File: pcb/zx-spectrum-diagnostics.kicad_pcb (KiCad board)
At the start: 2 copper layers, 13 parts, among them J101 Conn_01x04, U101 Pico, U102 Pico

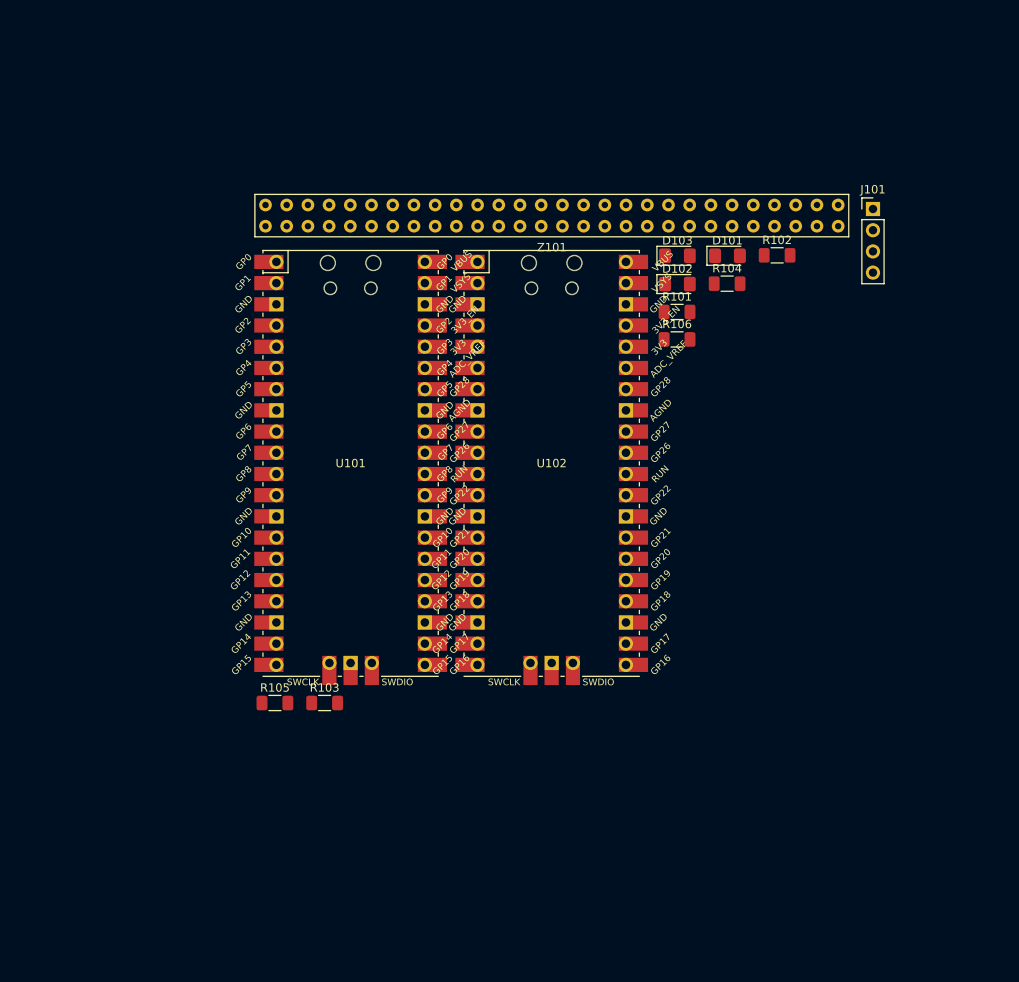
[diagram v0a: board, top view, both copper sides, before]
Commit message: back out previous layout, rearrange connections to match edge connector
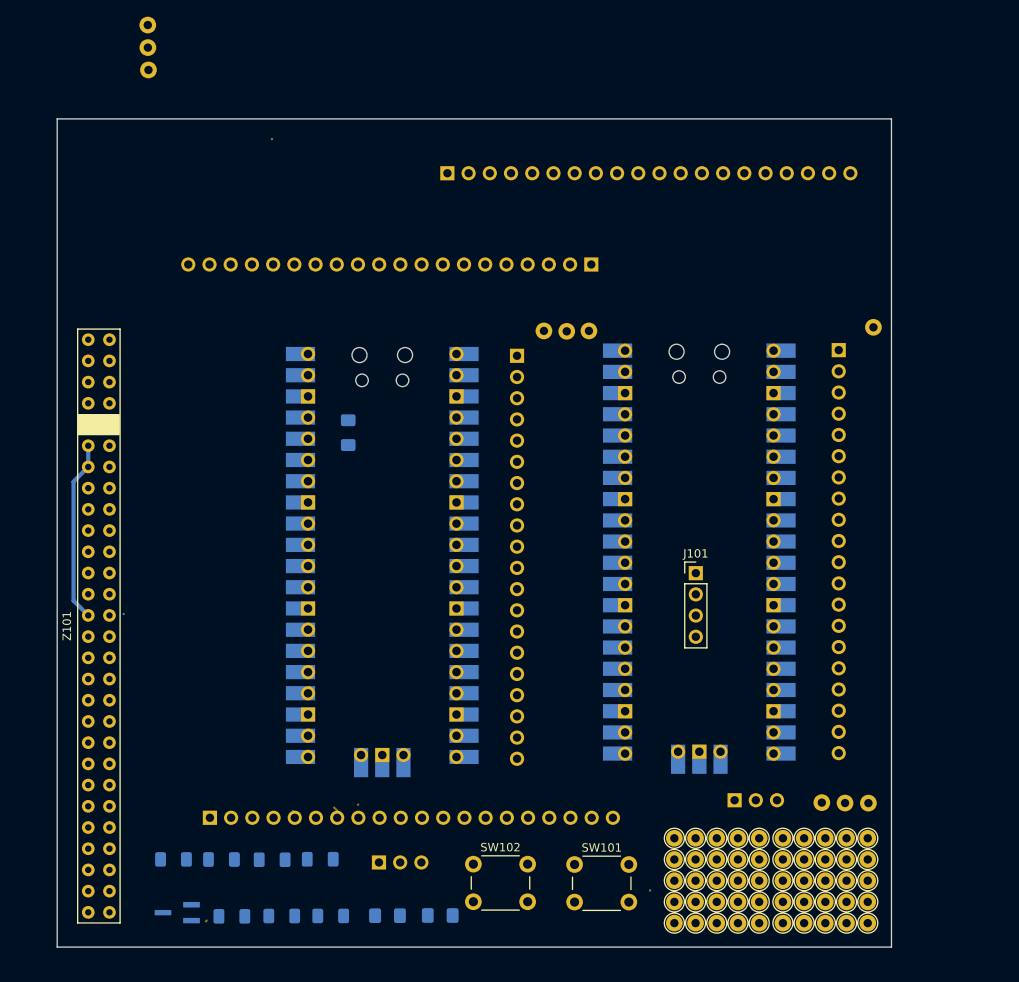
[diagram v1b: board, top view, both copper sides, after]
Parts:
- added ?: , , F.Cu at (133.0, 80.3)
- added ?: , , F.Cu at (172.4, 79.8)
- added ?: , , F.Cu at (85.6, 49.0)
- added ?: , , F.Cu at (166.3, 136.8)
- added ?: , , F.Cu at (85.5, 43.6)
- added ?: , , F.Cu at (171.8, 136.8)
- added ?: , , F.Cu at (138.4, 80.3)
- added ?: , , F.Cu at (135.7, 80.3)
- added ?: , , F.Cu at (169.1, 136.8)
- added ?: , , F.Cu at (85.6, 46.3)
- added J102: Conn_01x03_Male, Connector_PinSocket_2.54mm:PinSocket_1x03_P2.54mm_Vertical, B.Cu at (155.8, 136.5)
- added J103: Conn_01x03_Male, Connector_PinSocket_2.54mm:PinSocket_1x03_P2.54mm_Vertical, B.Cu at (113.2, 143.9)
- added J201: Conn_01x20_Female, Connector_PinSocket_2.54mm:PinSocket_1x20_P2.54mm_Vertical, B.Cu at (138.7, 72.3)
- added J202: Conn_01x20_Female, Connector_PinSocket_2.54mm:PinSocket_1x20_P2.54mm_Vertical, B.Cu at (93.0, 138.6)
- added J203: Conn_01x20_Female, Connector_PinSocket_2.54mm:PinSocket_1x20_P2.54mm_Vertical, B.Cu at (121.4, 61.4)
- added J204: Conn_01x20_Female, Connector_PinSocket_2.54mm:PinSocket_1x20_P2.54mm_Vertical, B.Cu at (168.3, 82.6)
- added J205: Conn_01x20_Female, Connector_PinSocket_2.54mm:PinSocket_1x20_P2.54mm_Vertical, B.Cu at (129.8, 83.2)
- added Q101: PMBT2222A, Package_TO_SOT_SMD:TSOT-23_HandSoldering, B.Cu at (89.1, 149.9)
- added R107: 1K, Resistor_SMD:R_1206_3216Metric_Pad1.30x1.75mm_HandSolder, B.Cu at (95.6, 150.4)
- added REF**: TestPoint_THTPad_D2.0mm_Drill1.0mm, TestPoint:TestPoint_THTPad_D2.0mm_Drill1.0mm, F.Cu at (148.6, 141.0)
- added REF**: TestPoint_THTPad_D2.0mm_Drill1.0mm, TestPoint:TestPoint_THTPad_D2.0mm_Drill1.0mm, F.Cu at (161.6, 141.0)
- added REF**1: TestPoint_THTPad_D2.0mm_Drill1.0mm, TestPoint:TestPoint_THTPad_D2.0mm_Drill1.0mm, F.Cu at (151.2, 141.0)
- added REF**1: TestPoint_THTPad_D2.0mm_Drill1.0mm, TestPoint:TestPoint_THTPad_D2.0mm_Drill1.0mm, F.Cu at (164.2, 141.0)
- added REF**10: TestPoint_THTPad_D2.0mm_Drill1.0mm, TestPoint:TestPoint_THTPad_D2.0mm_Drill1.0mm, F.Cu at (148.6, 146.1)
- added REF**10: TestPoint_THTPad_D2.0mm_Drill1.0mm, TestPoint:TestPoint_THTPad_D2.0mm_Drill1.0mm, F.Cu at (161.6, 146.1)
- added REF**11: TestPoint_THTPad_D2.0mm_Drill1.0mm, TestPoint:TestPoint_THTPad_D2.0mm_Drill1.0mm, F.Cu at (164.2, 146.1)
- added REF**11: TestPoint_THTPad_D2.0mm_Drill1.0mm, TestPoint:TestPoint_THTPad_D2.0mm_Drill1.0mm, F.Cu at (151.2, 146.1)
- added REF**12: TestPoint_THTPad_D2.0mm_Drill1.0mm, TestPoint:TestPoint_THTPad_D2.0mm_Drill1.0mm, F.Cu at (166.7, 146.1)
- added REF**12: TestPoint_THTPad_D2.0mm_Drill1.0mm, TestPoint:TestPoint_THTPad_D2.0mm_Drill1.0mm, F.Cu at (153.7, 146.1)
- added REF**13: TestPoint_THTPad_D2.0mm_Drill1.0mm, TestPoint:TestPoint_THTPad_D2.0mm_Drill1.0mm, F.Cu at (156.2, 146.1)
- added REF**13: TestPoint_THTPad_D2.0mm_Drill1.0mm, TestPoint:TestPoint_THTPad_D2.0mm_Drill1.0mm, F.Cu at (169.2, 146.1)
- added REF**14: TestPoint_THTPad_D2.0mm_Drill1.0mm, TestPoint:TestPoint_THTPad_D2.0mm_Drill1.0mm, F.Cu at (171.8, 146.1)
- added REF**14: TestPoint_THTPad_D2.0mm_Drill1.0mm, TestPoint:TestPoint_THTPad_D2.0mm_Drill1.0mm, F.Cu at (158.8, 146.1)
- added REF**15: TestPoint_THTPad_D2.0mm_Drill1.0mm, TestPoint:TestPoint_THTPad_D2.0mm_Drill1.0mm, F.Cu at (161.6, 148.6)
- added REF**15: TestPoint_THTPad_D2.0mm_Drill1.0mm, TestPoint:TestPoint_THTPad_D2.0mm_Drill1.0mm, F.Cu at (148.6, 148.6)
- added REF**16: TestPoint_THTPad_D2.0mm_Drill1.0mm, TestPoint:TestPoint_THTPad_D2.0mm_Drill1.0mm, F.Cu at (164.2, 148.6)
- added REF**16: TestPoint_THTPad_D2.0mm_Drill1.0mm, TestPoint:TestPoint_THTPad_D2.0mm_Drill1.0mm, F.Cu at (151.2, 148.6)
- added REF**17: TestPoint_THTPad_D2.0mm_Drill1.0mm, TestPoint:TestPoint_THTPad_D2.0mm_Drill1.0mm, F.Cu at (166.7, 148.6)
- added REF**17: TestPoint_THTPad_D2.0mm_Drill1.0mm, TestPoint:TestPoint_THTPad_D2.0mm_Drill1.0mm, F.Cu at (153.7, 148.6)
- added REF**18: TestPoint_THTPad_D2.0mm_Drill1.0mm, TestPoint:TestPoint_THTPad_D2.0mm_Drill1.0mm, F.Cu at (156.2, 148.6)
- added REF**18: TestPoint_THTPad_D2.0mm_Drill1.0mm, TestPoint:TestPoint_THTPad_D2.0mm_Drill1.0mm, F.Cu at (169.2, 148.6)
- added REF**19: TestPoint_THTPad_D2.0mm_Drill1.0mm, TestPoint:TestPoint_THTPad_D2.0mm_Drill1.0mm, F.Cu at (158.8, 148.6)
- added REF**19: TestPoint_THTPad_D2.0mm_Drill1.0mm, TestPoint:TestPoint_THTPad_D2.0mm_Drill1.0mm, F.Cu at (171.8, 148.6)
- added REF**2: TestPoint_THTPad_D2.0mm_Drill1.0mm, TestPoint:TestPoint_THTPad_D2.0mm_Drill1.0mm, F.Cu at (166.7, 141.0)
- added REF**2: TestPoint_THTPad_D2.0mm_Drill1.0mm, TestPoint:TestPoint_THTPad_D2.0mm_Drill1.0mm, F.Cu at (153.7, 141.0)
- added REF**20: TestPoint_THTPad_D2.0mm_Drill1.0mm, TestPoint:TestPoint_THTPad_D2.0mm_Drill1.0mm, F.Cu at (148.6, 151.2)
- added REF**20: TestPoint_THTPad_D2.0mm_Drill1.0mm, TestPoint:TestPoint_THTPad_D2.0mm_Drill1.0mm, F.Cu at (161.6, 151.2)
- added REF**21: TestPoint_THTPad_D2.0mm_Drill1.0mm, TestPoint:TestPoint_THTPad_D2.0mm_Drill1.0mm, F.Cu at (151.2, 151.2)
- added REF**21: TestPoint_THTPad_D2.0mm_Drill1.0mm, TestPoint:TestPoint_THTPad_D2.0mm_Drill1.0mm, F.Cu at (164.2, 151.2)
- added REF**22: TestPoint_THTPad_D2.0mm_Drill1.0mm, TestPoint:TestPoint_THTPad_D2.0mm_Drill1.0mm, F.Cu at (166.7, 151.2)
- added REF**22: TestPoint_THTPad_D2.0mm_Drill1.0mm, TestPoint:TestPoint_THTPad_D2.0mm_Drill1.0mm, F.Cu at (153.7, 151.2)
- added REF**23: TestPoint_THTPad_D2.0mm_Drill1.0mm, TestPoint:TestPoint_THTPad_D2.0mm_Drill1.0mm, F.Cu at (169.2, 151.2)
- added REF**23: TestPoint_THTPad_D2.0mm_Drill1.0mm, TestPoint:TestPoint_THTPad_D2.0mm_Drill1.0mm, F.Cu at (156.2, 151.2)
- added REF**24: TestPoint_THTPad_D2.0mm_Drill1.0mm, TestPoint:TestPoint_THTPad_D2.0mm_Drill1.0mm, F.Cu at (158.8, 151.2)
- added REF**24: TestPoint_THTPad_D2.0mm_Drill1.0mm, TestPoint:TestPoint_THTPad_D2.0mm_Drill1.0mm, F.Cu at (171.8, 151.2)
- added REF**3: TestPoint_THTPad_D2.0mm_Drill1.0mm, TestPoint:TestPoint_THTPad_D2.0mm_Drill1.0mm, F.Cu at (169.2, 141.0)
- added REF**3: TestPoint_THTPad_D2.0mm_Drill1.0mm, TestPoint:TestPoint_THTPad_D2.0mm_Drill1.0mm, F.Cu at (156.2, 141.0)
- added REF**4: TestPoint_THTPad_D2.0mm_Drill1.0mm, TestPoint:TestPoint_THTPad_D2.0mm_Drill1.0mm, F.Cu at (158.8, 141.0)
- added REF**4: TestPoint_THTPad_D2.0mm_Drill1.0mm, TestPoint:TestPoint_THTPad_D2.0mm_Drill1.0mm, F.Cu at (171.8, 141.0)
- added REF**5: TestPoint_THTPad_D2.0mm_Drill1.0mm, TestPoint:TestPoint_THTPad_D2.0mm_Drill1.0mm, F.Cu at (148.6, 143.6)
- added REF**5: TestPoint_THTPad_D2.0mm_Drill1.0mm, TestPoint:TestPoint_THTPad_D2.0mm_Drill1.0mm, F.Cu at (161.6, 143.6)
- added REF**6: TestPoint_THTPad_D2.0mm_Drill1.0mm, TestPoint:TestPoint_THTPad_D2.0mm_Drill1.0mm, F.Cu at (164.2, 143.6)
- added REF**6: TestPoint_THTPad_D2.0mm_Drill1.0mm, TestPoint:TestPoint_THTPad_D2.0mm_Drill1.0mm, F.Cu at (151.2, 143.6)
- added REF**7: TestPoint_THTPad_D2.0mm_Drill1.0mm, TestPoint:TestPoint_THTPad_D2.0mm_Drill1.0mm, F.Cu at (166.7, 143.6)
- added REF**7: TestPoint_THTPad_D2.0mm_Drill1.0mm, TestPoint:TestPoint_THTPad_D2.0mm_Drill1.0mm, F.Cu at (153.7, 143.6)
- added REF**8: TestPoint_THTPad_D2.0mm_Drill1.0mm, TestPoint:TestPoint_THTPad_D2.0mm_Drill1.0mm, F.Cu at (169.2, 143.6)
- added REF**8: TestPoint_THTPad_D2.0mm_Drill1.0mm, TestPoint:TestPoint_THTPad_D2.0mm_Drill1.0mm, F.Cu at (156.2, 143.6)
- added REF**9: TestPoint_THTPad_D2.0mm_Drill1.0mm, TestPoint:TestPoint_THTPad_D2.0mm_Drill1.0mm, F.Cu at (158.8, 143.6)
- added REF**9: TestPoint_THTPad_D2.0mm_Drill1.0mm, TestPoint:TestPoint_THTPad_D2.0mm_Drill1.0mm, F.Cu at (171.8, 143.6)
- added SW101: SW_SPST, Button_Switch_THT:SW_PUSH_6mm_H4.3mm, F.Cu at (136.7, 144.2)
- added SW102: SW_SPST, Button_Switch_THT:SW_PUSH_6mm_H4.3mm, F.Cu at (124.5, 144.1)
- D101, D102, D103, R101, R102, R103, R104, R105, R106, U101, U102: moved to B.Cu
- moved R102 95.5 mm to (107.5, 150.3)
- moved R101 86.5 mm to (101.6, 150.3), turned to 180 degrees
- moved R104 84.4 mm to (106.2, 143.5)
- moved D103 84.0 mm to (120.6, 150.3), turned to 180 degrees
- moved D102 83.2 mm to (114.3, 150.3), turned to 180 degrees
- moved R106 82.8 mm to (94.4, 143.6)
- moved Z101 73.2 mm to (79.7, 115.6), turned to -90 degrees
- moved D101 50.1 mm to (109.5, 92.4), turned to -90 degrees
- moved J101 48.5 mm to (151.2, 109.3)
- moved U101 43.1 mm to (151.6, 106.8), turned to 180 degrees
- moved U102 23.1 mm to (113.6, 107.2), turned to 180 degrees
- moved R105 22.3 mm to (88.6, 143.6), turned to 180 degrees
- moved R103 19.8 mm to (100.4, 143.6), turned to 180 degrees
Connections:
- U101 pad 1: P2_LINKOUT -> P1_GPIO0
- U101 pad 10: unconnected-(U101-Pad10) -> P1_GPIO7
- U101 pad 11: unconnected-(U101-Pad11) -> P1_GPIO8
- U101 pad 12: unconnected-(U101-Pad12) -> P1_GPIO9
- U101 pad 13: unconnected-(U101-Pad13) -> GND
- U101 pad 14: unconnected-(U101-Pad14) -> P1_GPIO10
- U101 pad 15: unconnected-(U101-Pad15) -> P1_GPIO11
- U101 pad 16: unconnected-(U101-Pad16) -> P1_GPIO12
- U101 pad 17: unconnected-(U101-Pad17) -> P1_GPIO13
- U101 pad 18: unconnected-(U101-Pad18) -> GND
- U101 pad 19: unconnected-(U101-Pad19) -> P1_GPIO14
- U101 pad 2: P2_LINKIN -> P1_GPIO1
- U101 pad 20: unconnected-(U101-Pad20) -> P1_GPIO15
- U101 pad 21: unconnected-(U101-Pad21) -> OLED_SDA
- U101 pad 22: unconnected-(U101-Pad22) -> OLED_SCK
- U101 pad 23: unconnected-(U101-Pad23) -> GND
- U101 pad 24: unconnected-(U101-Pad24) -> P2_LINKOUT
- U101 pad 25: unconnected-(U101-Pad25) -> P2_LINKIN
- U101 pad 26: unconnected-(U101-Pad26) -> INPUT2
- U101 pad 27: unconnected-(U101-Pad27) -> INPUT1
- U101 pad 28: unconnected-(U101-Pad28) -> GND
- U101 pad 29: unconnected-(U101-Pad29) -> PICO_RESET_Z80
- U101 pad 3: unconnected-(U101-Pad3) -> GND
- U101 pad 33: unconnected-(U101-Pad33) -> GND
- U101 pad 38: unconnected-(U101-Pad38) -> GND
- U101 pad 4: OLED_SDA -> P1_GPIO2
- U101 pad 41: unconnected-(U101-Pad41) -> P1_SWCLK
- U101 pad 42: unconnected-(U101-Pad42) -> GND
- U101 pad 43: unconnected-(U101-Pad43) -> P1_SWDIO
- U101 pad 5: OLED_SCK -> P1_GPIO3
- U101 pad 6: unconnected-(U101-Pad6) -> P1_GPIO4
- U101 pad 7: unconnected-(U101-Pad7) -> P1_GPIO5
- U101 pad 8: unconnected-(U101-Pad8) -> GND
- U101 pad 9: unconnected-(U101-Pad9) -> P1_GPIO6
- U102 pad 1: unconnected-(U102-Pad1) -> P2_GPIO0
- U102 pad 10: unconnected-(U102-Pad10) -> P2_GPIO7
- U102 pad 11: unconnected-(U102-Pad11) -> P2_GPIO8
- U102 pad 12: unconnected-(U102-Pad12) -> P2_GPIO9
- U102 pad 13: unconnected-(U102-Pad13) -> GND
- U102 pad 14: unconnected-(U102-Pad14) -> P2_GPIO10
- U102 pad 15: unconnected-(U102-Pad15) -> P2_GPIO11
- U102 pad 16: unconnected-(U102-Pad16) -> P2_GPIO12
- U102 pad 17: unconnected-(U102-Pad17) -> P2_GPIO13
- U102 pad 18: unconnected-(U102-Pad18) -> GND
- U102 pad 19: unconnected-(U102-Pad19) -> P2_GPIO14
- U102 pad 2: unconnected-(U102-Pad2) -> P2_GPIO1
- U102 pad 20: unconnected-(U102-Pad20) -> P2_GPIO15
- U102 pad 21: unconnected-(U102-Pad21) -> P2_GPIO16
- U102 pad 22: unconnected-(U102-Pad22) -> P2_GPIO17
- U102 pad 23: unconnected-(U102-Pad23) -> GND
- U102 pad 24: unconnected-(U102-Pad24) -> P2_GPIO18
- U102 pad 25: unconnected-(U102-Pad25) -> P2_GPIO19
- U102 pad 26: unconnected-(U102-Pad26) -> P2_GPIO20
- U102 pad 28: unconnected-(U102-Pad28) -> GND
- U102 pad 3: unconnected-(U102-Pad3) -> GND
- U102 pad 31: unconnected-(U102-Pad31) -> P2_GPIO26
- U102 pad 32: unconnected-(U102-Pad32) -> P2_GPIO27
- U102 pad 33: unconnected-(U102-Pad33) -> GND
- U102 pad 34: unconnected-(U102-Pad34) -> P2_GPIO28
- U102 pad 38: unconnected-(U102-Pad38) -> GND
- U102 pad 4: unconnected-(U102-Pad4) -> P2_GPIO2
- U102 pad 41: unconnected-(U102-Pad41) -> P2_SWCLK
- U102 pad 42: unconnected-(U102-Pad42) -> GND
- U102 pad 43: unconnected-(U102-Pad43) -> P2_SWDIO
- U102 pad 5: unconnected-(U102-Pad5) -> P2_GPIO3
- U102 pad 6: unconnected-(U102-Pad6) -> P2_GPIO4
- U102 pad 7: unconnected-(U102-Pad7) -> P2_GPIO5
- U102 pad 8: unconnected-(U102-Pad8) -> GND
- U102 pad 9: unconnected-(U102-Pad9) -> P2_GPIO6
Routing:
- net GND: track 0.00 -> 22.2 mm
- net ZXY: track 0.00 -> 1.53 mm
- net ZXD6: track 0.00 -> 0.67 mm
- net ZXBUSRQ: track 0.00 -> 0.64 mm
- net ZXM1: track 0.00 -> 0.62 mm
- net ZXMIN5V: track 0.00 -> 0.61 mm
- net ZXU: track 0.00 -> 0.53 mm
- net ZXNMI: track 0.00 -> 0.50 mm
- net ZXHALT: track 0.00 -> 0.50 mm
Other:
- board outline added: 99.9 x 99.2 mm
- board text added: "+9V"
- board text added: "-5V"
- board text added: "-5V_DIV"
- board text added: "12V"
- board text added: "12VAC"
- board text added: "12V_DIV"
- board text added: "5V_DIV"
- board text added: "A0"
- board text added: "A1"
- board text added: "A10"
- board text added: "A11"
- board text added: "A12"
- board text added: "A13"
- board text added: "A14"
- board text added: "A15"
- board text added: "A2"
- board text added: "A3"
- board text added: "A4"
- board text added: "A5"
- board text added: "A6"
- board text added: "A7"
- board text added: "A8"
- board text added: "A9"
- board text added: "B'ACK"
- board text added: "BUSRQ"
- board text added: "CLK"
- board text added: "D0"
- board text added: "D1"
- board text added: "D2"
- board text added: "D3"
- board text added: "D4"
- board text added: "D5"
- board text added: "D6"
- board text added: "D7"
- board text added: "GP0"
- board text added: "GP10"
- board text added: "GP12"
- board text added: "GP14"
- board text added: "GP15"
- board text added: "GP2"
- board text added: "GP4"
- board text added: "GP6"
- board text added: "GP8"
- board text added: "HALT"
- board text added: "INT"
- board text added: "IORQ"
- board text added: "IORQGE"
- board text added: "M1"
- board text added: "MREQ"
- board text added: "NMI"
- board text added: "P2-0"
- board text added: "P2-1"
- board text added: "P2-10"
- board text added: "P2-12"
- board text added: "P2-14"
- board text added: "P2-16"
- board text added: "P2-18"
- board text added: "P2-2"
- board text added: "P2-20"
- board text added: "P2-26"
- board text added: "P2-27"
- board text added: "P2-28"
- board text added: "P2-3"
- board text added: "P2-4"
- board text added: "P2-6"
- board text added: "P2-8"
- board text added: "RD"
- board text added: "RESET"
- board text added: "RFSH"
- board text added: "ROMCS"
- board text added: "U"
- board text added: "V"
- board text added: "VIDEO"
- board text added: "WAIT"
- board text added: "WR"
- board text added: "Y"

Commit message: relaid, complete, needs tidying
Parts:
- added ?: , , F.Cu at (158.9, 76.4)
- added ?: , , F.Cu at (155.9, 76.4)
- added ?: , , F.Cu at (162.0, 76.4)
- added ?: , , F.Cu at (164.8, 76.4)
- moved J201 45.5 mm to (94.1, 81.4), turned to 180 degrees
- moved J203 40.4 mm to (86.4, 81.5), turned to 180 degrees
- moved ? 38.2 mm to (102.3, 77.9), turned to -90 degrees
- moved ? 37.3 mm to (105.3, 77.9), turned to -90 degrees
- moved ? 32.0 mm to (99.2, 78.0), turned to -90 degrees
- moved ? 23.4 mm to (109.7, 77.9)
- moved ? 23.1 mm to (112.7, 77.9)
- moved ? 22.7 mm to (115.8, 77.9)
- moved SW102 7.92 mm to (130.9, 148.8), turned to 180 degrees
- moved SW101 7.81 mm to (143.1, 148.5), turned to 180 degrees
- moved ? 5.74 mm to (167.8, 76.4)
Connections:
- J201 pad 1: ZXA0 -> ZXA15
- J201 pad 10: ZXA9 -> ZXD4
- J201 pad 11: ZXA10 -> ZXINT
- J201 pad 12: ZXA11 -> ZXNMI
- J201 pad 13: ZXA12 -> ZXHALT
- J201 pad 14: ZXA13 -> ZXMREQ
- J201 pad 15: ZXA14 -> ZXIORQ
- J201 pad 16: ZXA15 -> ZXRD
- J201 pad 17: ZXINT -> ZXWR
- J201 pad 18: ZXNMI -> ZXMIN5V
- J201 pad 19: ZXHALT -> ZXWAIT
- J201 pad 2: ZXA1 -> ZXA13
- J201 pad 20: ZXMREQ -> ZX12V
- J201 pad 3: ZXA2 -> ZXD7
- J201 pad 4: ZXA3 -> ZXD0
- J201 pad 5: ZXA4 -> ZXD1
- J201 pad 6: ZXA5 -> ZXD2
- J201 pad 7: ZXA6 -> ZXD6
- J201 pad 8: ZXA7 -> ZXD5
- J201 pad 9: ZXA8 -> ZXD3
- J202 pad 1: ZX9V -> ZXROMCS
- J202 pad 10: 12V_DIV -> 5V_DIV
- J202 pad 11: MIN5V_DIV -> 12V_DIV
- J202 pad 12: unconnected-(J202-Pad12) -> MIN5V_DIV
- J202 pad 2: ZXCLK -> ZXBUSACK
- J202 pad 3: ZXIORQGE -> ZXA9
- J202 pad 4: ZXVIDEO -> ZXA11
- J202 pad 5: ZXY -> ZX12VAC
- J202 pad 6: ZXV -> ZXM1
- J202 pad 7: ZXU -> ZXRFSH
- J202 pad 8: ZXBUSRQ -> ZXA8
- J202 pad 9: 5V_DIV -> ZXA10
- J203 pad 1: ZXD0 -> ZXA14
- J203 pad 10: ZXRD -> ZXIORQGE
- J203 pad 11: ZXWR -> ZXVIDEO
- J203 pad 12: ZXMIN5V -> ZXY
- J203 pad 13: ZXWAIT -> ZXV
- J203 pad 14: ZX12V -> ZXU
- J203 pad 15: ZX12VAC -> ZXBUSRQ
- J203 pad 16: ZXM1 -> ZXRESET
- J203 pad 17: ZXRFSH -> ZXA7
- J203 pad 18: ZXRESET -> ZXA6
- J203 pad 19: ZXROMCS -> ZXA5
- J203 pad 2: ZXD1 -> ZXA12
- J203 pad 20: ZXBUSACK -> ZXA4
- J203 pad 3: ZXD2 -> +5V
- J203 pad 4: ZXD3 -> ZX9V
- J203 pad 5: ZXD4 -> ZXCLK
- J203 pad 6: ZXD5 -> ZXA0
- J203 pad 7: ZXD6 -> ZXA1
- J203 pad 8: ZXD7 -> ZXA2
- J203 pad 9: ZXIORQ -> ZXA3
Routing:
- net +5V: track 0.00 -> 213.6 mm, vias 0 -> 7
- net 3V3_PICO1: track 0.00 -> 165.4 mm, vias 0 -> 8
- net P2_GPIO3: track 0.00 -> 124.9 mm, vias 0 -> 3
- net P2_GPIO2: track 0.00 -> 116.3 mm, vias 0 -> 3
- net P2_GPIO1: track 0.00 -> 104.3 mm, vias 0 -> 2
- net 12V_DIV: track 0.00 -> 97.5 mm, vias 0 -> 4
- net P2_GPIO0: track 0.00 -> 95.2 mm, vias 0 -> 2
- net MIN5V_DIV: track 0.00 -> 94.4 mm, vias 0 -> 6
- net 5V_DIV: track 0.00 -> 94.1 mm, vias 0 -> 5
- net PICO_RESET_Z80: track 0.00 -> 89.3 mm, vias 0 -> 3
- net P2_LINKOUT: track 0.00 -> 71.7 mm, vias 0 -> 4
- net P2_LINKIN: track 0.00 -> 68.0 mm, vias 0 -> 4
- net P2_GPIO28: track 0.00 -> 65.6 mm, vias 0 -> 1
- net PICO_PWR: track 0.00 -> 59.6 mm, vias 0 -> 5
- net ZXMIN5V: track 0.61 -> 57.4 mm, vias 0 -> 3
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- added copper zone on F.Cu, net GND

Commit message: lots more tidyups, nearly done
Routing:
- net P2_GPIO27: track 56.4 -> 51.4 mm
- net 12V_DIV: track 97.5 -> 95.4 mm
- net ZX12VAC: track 24.3 -> 22.7 mm
- net PICO_PWR: track 59.6 -> 58.0 mm
- net INPUT2: track 45.3 -> 43.7 mm
- net P2_GPIO28: track 65.6 -> 64.0 mm
- net P1_GPIO15: track 14.4 -> 12.8 mm
- net P1_GPIO14: track 14.4 -> 12.8 mm
- net P1_GPIO13: track 12.0 -> 10.4 mm
- net P1_GPIO12: track 11.9 -> 10.3 mm
- net P1_GPIO11: track 11.9 -> 10.3 mm
- net P1_GPIO10: track 11.9 -> 10.3 mm
- net ZXD6: track 15.9 -> 15.2 mm
- net ZXMIN5V: track 57.4 -> 56.8 mm
- net ZXM1: track 25.9 -> 25.2 mm
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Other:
- board size 99.9 x 99.2 mm -> 99.9 x 79.9 mm
- board text added: "+5V"
- board text added: "BUSACK"
- board text added: "P1-0"
- board text added: "P1-1"
- board text added: "P1-10"
- board text added: "P1-11"
- board text added: "P1-12"
- board text added: "P1-13"
- board text added: "P1-14"
- board text added: "P1-15"
- board text added: "P1-2"
- board text added: "P1-3"
- board text added: "P1-4"
- board text added: "P1-5"
- board text added: "P1-6"
- board text added: "P1-7"
- board text added: "P1-8"
- board text added: "P1-9"
- board text added: "P2-11"
- board text added: "P2-13"
- board text added: "P2-15"
- board text added: "P2-17"
- board text added: "P2-19"
- board text added: "P2-5"
- board text added: "P2-7"
- board text added: "P2-9"
- board text removed: "B'ACK"
- board text removed: "GP0"
- board text removed: "GP10"
- board text removed: "GP12"
- board text removed: "GP14"
- board text removed: "GP15"
- board text removed: "GP2"
- board text removed: "GP4"
- board text removed: "GP6"
- board text removed: "GP8"

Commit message: final, ready for fab
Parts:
- moved J101 7.53 mm to (151.1, 116.8), turned to 180 degrees
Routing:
- net OLED_SDA: track 35.5 -> 27.9 mm
- net ZX9V: track 8.91 -> 12.2 mm
- net OLED_SCK: track 28.2 -> 25.8 mm
- net PICO_PWR: track 58.0 -> 59.8 mm
- net PICO_RESET_Z80: track 89.3 -> 90.1 mm
- net ZXA13: track 14.3 -> 13.6 mm
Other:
- board text added: "+3.3V"
- board text added: "GND"
- board text added: "GNDs"
- board text added: "OLED 3V3"
- board text added: "OLED GND"
- board text added: "OLED SCK"
- board text added: "OLED SDA"

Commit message: v1.0 off to fab
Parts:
- D102, D103: footprint Diode_SMD:D_1206_3216Metric_Pad1.42x1.75mm_HandSolder -> Diode_SMD:D_SOD-123
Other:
- board text added: "Some 3216 footprints with tracks coming from them might be more useful than all these test points? If I want to mount SMD diodes or something?"

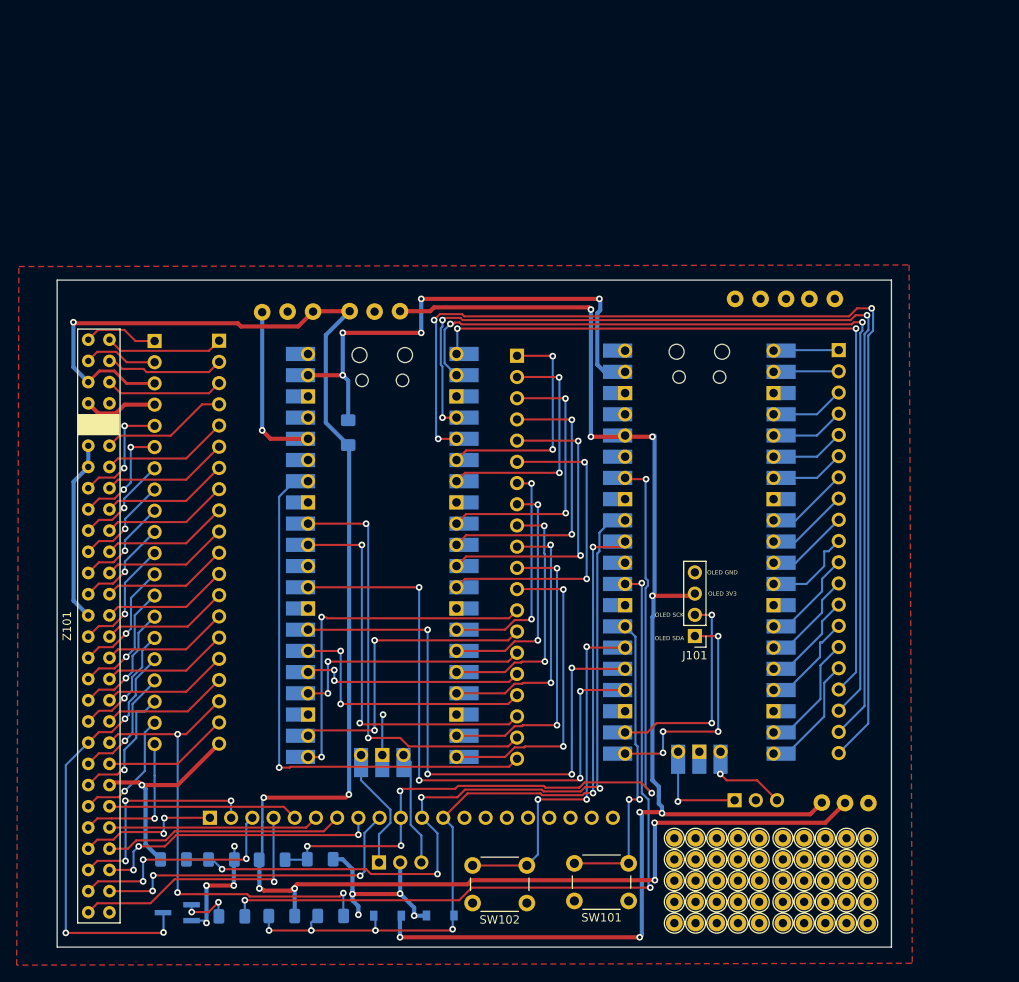
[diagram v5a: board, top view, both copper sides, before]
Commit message: change the layout to use the proper edge connector
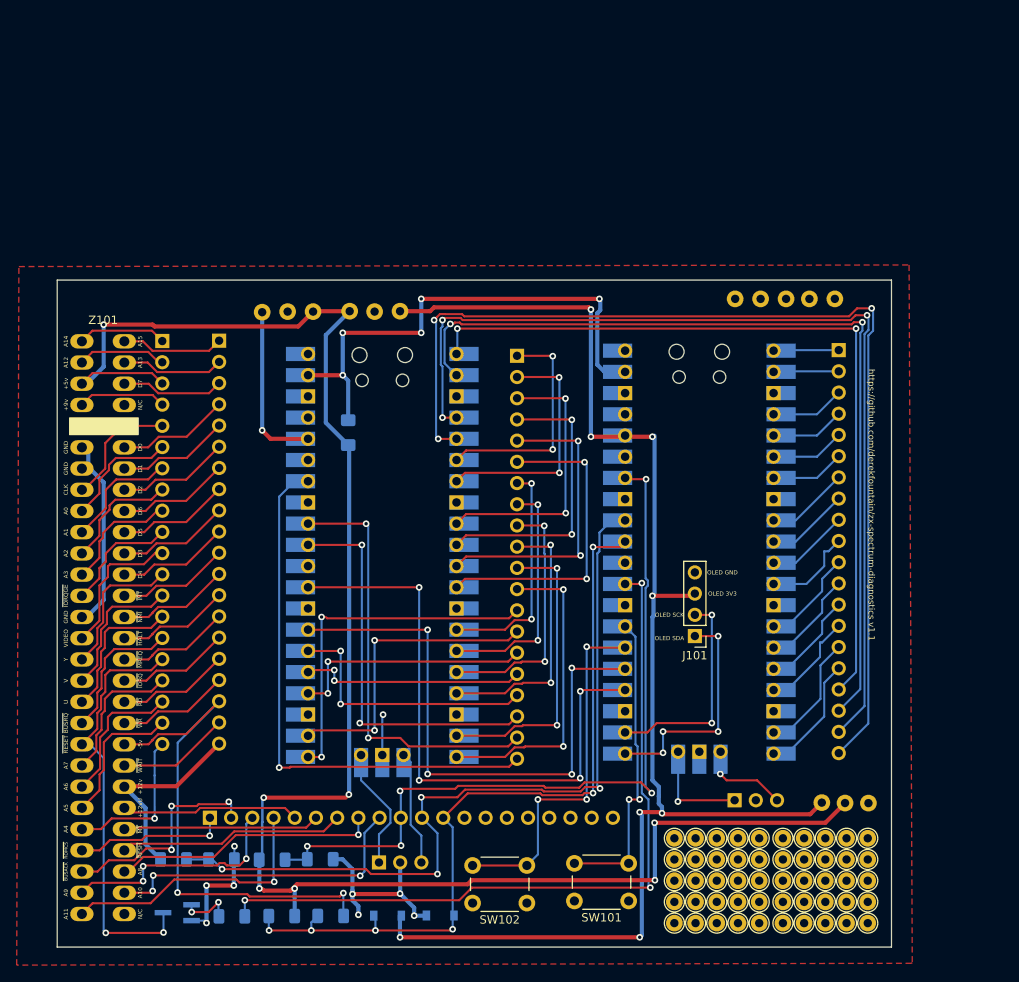
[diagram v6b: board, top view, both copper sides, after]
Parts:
- Z101: footprint zxbus:ZX_Bus_Pin_Header -> zxedge:Spectrum_Edge_Connector
- moved Z101 1.19 mm to (80.2, 114.5)
- moved J203 0.92 mm to (87.3, 81.5)
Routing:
- net ZXMIN5V: track 57.1 -> 61.4 mm, vias 3 -> 2
- net ZXA8: track 34.9 -> 31.4 mm, vias 3 -> 1
- net ZXA7: track 14.1 -> 16.9 mm, vias 1 -> 0
- net ZXY: track 14.2 -> 17.1 mm, vias 1 -> 0
- net ZXVIDEO: track 14.3 -> 17.1 mm, vias 1 -> 0
- net ZXU: track 14.4 -> 17.1 mm, vias 1 -> 0
- net ZXBUSRQ: track 14.2 -> 16.8 mm, vias 1 -> 0
- net ZXV: track 14.4 -> 16.9 mm, vias 1 -> 0
- net +5V: track 213.8 -> 211.4 mm
- net ZXA2: track 11.7 -> 14.1 mm, vias 1 -> 0
- net ZXIORQGE: track 11.7 -> 14.1 mm, vias 1 -> 0
- net ZXA5: track 14.8 -> 16.9 mm, vias 1 -> 0
- net ZXA1: track 11.7 -> 13.7 mm, vias 1 -> 0
- net ZXRESET: track 52.0 -> 50.0 mm, vias 3 -> 2
- net ZXA3: track 11.8 -> 13.6 mm, vias 1 -> 0
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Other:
- board text added: "https://github.com/derekfountain/zx-spectrum-diagnostics v1.1"
